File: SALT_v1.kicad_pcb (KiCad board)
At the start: 2 copper layers, 41.8 x 28 mm, 18 parts, among them J1 TC2050-IDC, U1 DWM3001C, U2 SON50P200X200X80-9N

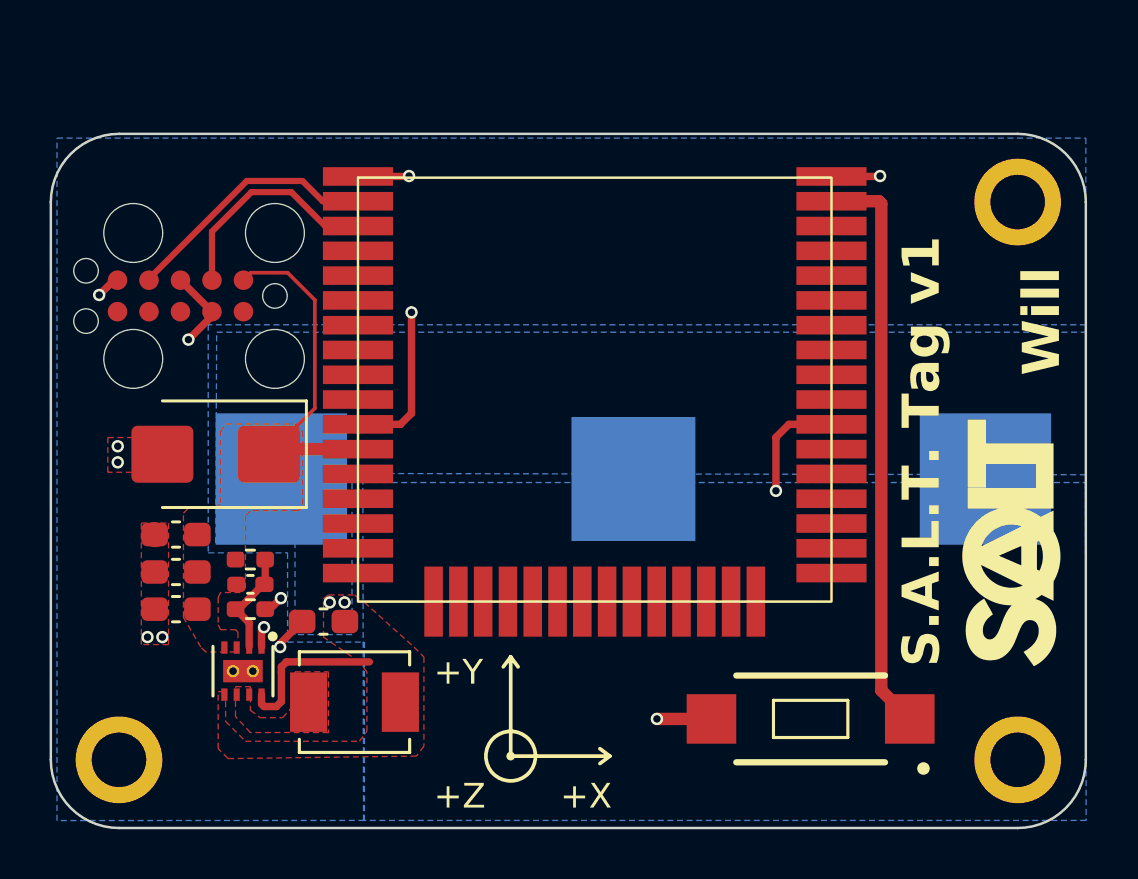
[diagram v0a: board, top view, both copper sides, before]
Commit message: Update SALT_v1.kicad_pcb
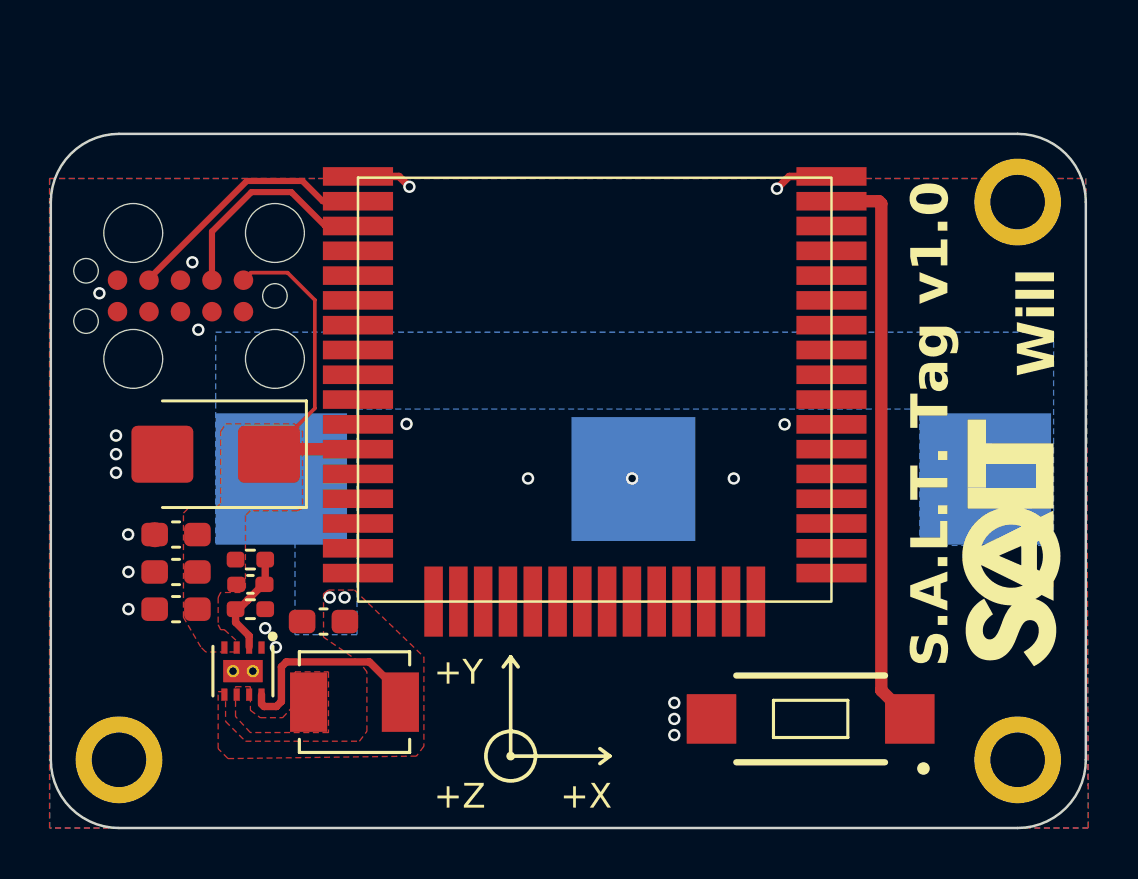
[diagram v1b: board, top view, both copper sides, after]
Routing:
- net GND: track 24.6 -> 4.67 mm, vias 14 -> 21
- net Net-(U2-EN): track 6.49 -> 8.63 mm
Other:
- board text added: "S.A.L.T. Tag v1.0"
- board text removed: "S.A.L.T. Tag v1"
